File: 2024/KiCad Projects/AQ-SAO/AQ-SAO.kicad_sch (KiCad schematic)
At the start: 13 parts, among them J1 SAO (on back), U1 74HC00, U2 74HC00

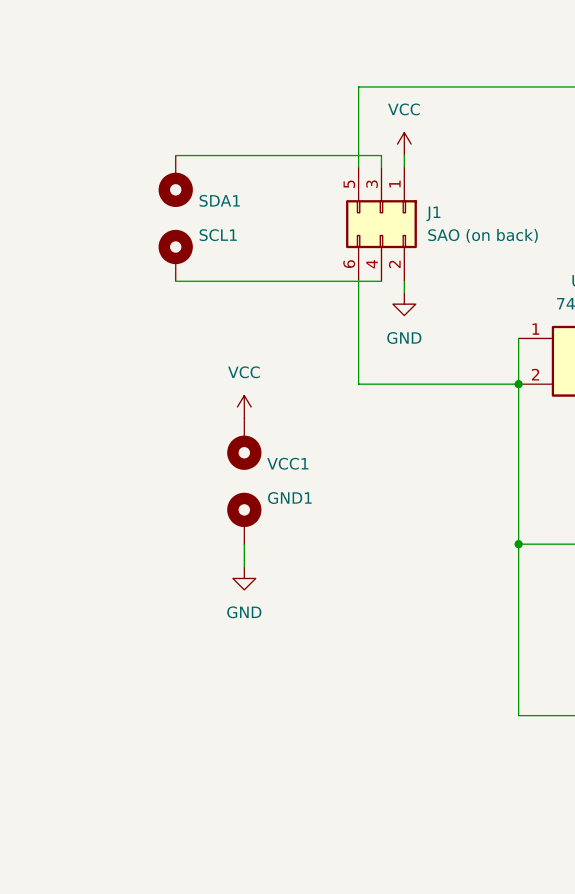
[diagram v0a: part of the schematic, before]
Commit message: Updating KiCad PCB files and README
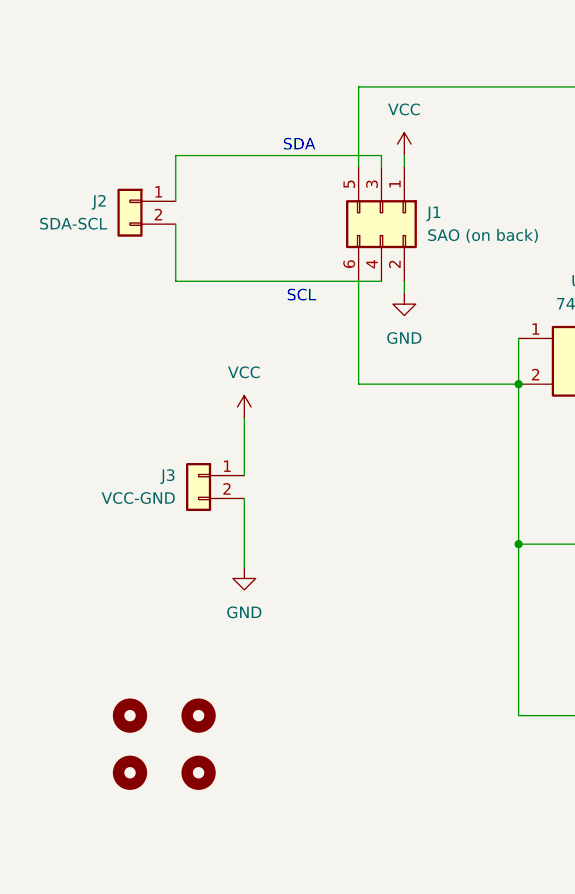
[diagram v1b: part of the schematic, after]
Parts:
- removed GND1: GND, TestPoint:TestPoint_THTPad_1.0x1.0mm_Drill0.5mm, symbol Mechanical:MountingHole_Pad
- removed SCL1: SCL, TestPoint:TestPoint_THTPad_1.0x1.0mm_Drill0.5mm, symbol Mechanical:MountingHole_Pad
- removed SDA1: SDA, TestPoint:TestPoint_THTPad_1.0x1.0mm_Drill0.5mm, symbol Mechanical:MountingHole_Pad
- removed VCC1: VCC, TestPoint:TestPoint_THTPad_1.0x1.0mm_Drill0.5mm, symbol Mechanical:MountingHole_Pad
- added H1, H2, H3, H4: MountingHole, MountingHole:MountingHole_2.2mm_M2, symbol Mechanical:MountingHole
- added J2: SDA-SCL, Connector_PinHeader_2.54mm:PinHeader_1x02_P2.54mm_Vertical, symbol Connector_Generic:Conn_01x02
- added J3: VCC-GND, Connector_PinHeader_2.54mm:PinHeader_1x02_P2.54mm_Vertical, symbol Connector_Generic:Conn_01x02
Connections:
- net GND: now also J3.2 (Pin_2)
- net VCC: now also J3.1 (Pin_1)
- net at J1.3 (Pin_3): now also J2.1 (Pin_1)
- net at J1.4 (Pin_4): now also J2.2 (Pin_2)
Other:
- note added: "SCL"
- note added: "SDA"
